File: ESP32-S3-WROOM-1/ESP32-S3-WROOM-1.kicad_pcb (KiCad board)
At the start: 2 copper layers, 25.4 x 57 mm, 23 parts, among them J1 ESP32-S3-DEVKITC-1-J1, J2 ESP32-S3-DEVKITC-1-J2, J3 UART, P1 USB2.0_C_12pin, SW1 BOOT, SW2 RESET, U1 ESP32-S3-WROOM-1, U2 AMS1117-3.3

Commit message: order
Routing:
- net GPIO8: track 18.3 -> 17.7 mm

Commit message: fix
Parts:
- removed P1: USB2.0_C_12pin, esp32-dev-boards:USB-C-12-Pin-MidMount
- added J4: USB2.0_C_v3, $74th:USB-C-12-Pin-MidMount-ali-v4, F.Cu at (77.5, 86.4)
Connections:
- D2 pad 2: GPIO20 -> GPIO19
- D3 pad 2: GPIO19 -> GPIO20
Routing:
- net GPIO19: track 66.4 -> 72.9 mm
- net GPIO20: track 68.1 -> 63.9 mm

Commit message: up
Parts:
- C1, C3, C4, C5, C6: footprint Capacitor_SMD:C_0805_2012Metric_Pad1.18x1.45mm_HandSolder -> esp32-dev-boards:Capacitor_0805_2012
- C2: value 100n -> 1u; footprint Capacitor_SMD:C_0805_2012Metric_Pad1.18x1.45mm_HandSolder -> esp32-dev-boards:Capacitor_0805_2012
- J3: value UART -> ESP-Prog-ProgramCOM-RECV; footprint esp32-dev-boards:UART -> $74th:BoxPinHeader_2x03_P1.27mm_Vertical
- R1, R2, R4: footprint Resistor_SMD:R_0805_2012Metric_Pad1.20x1.40mm_HandSolder -> esp32-dev-boards:Register_0805_2012
- R3: value 5.1k -> 1k; footprint Resistor_SMD:R_0805_2012Metric_Pad1.20x1.40mm_HandSolder -> esp32-dev-boards:Register_0805_2012
- moved J3 8.83 mm to (78.7, 79.2), turned to 90 degrees
- moved D1 5.56 mm to (85.0, 78.6), turned to 90 degrees
- moved D4 2.44 mm to (71.8, 80.5), turned to -90 degrees
- moved U2 0.23 mm to (74.5, 72.8)
- moved D3 0.12 mm to (83.7, 84.4)
- moved C2 0.06 mm to (82.1, 60.3)
- moved C4 0.06 mm to (68.9, 83.6)
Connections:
- J3 pad 1: U0TXD -> CHIP_PU
- J3 pad 2: U0RXD -> +5V
- J3 pad 3: +5V -> U0RXD
- J3 pad 5: CHIP_PU -> U0TXD
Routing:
- net Net-(D1-Pad2): track 12.8 -> 24.1 mm
- net U0TXD: track 55.6 -> 47.8 mm
- net GND: track 4.60 -> 11.2 mm, vias 14 -> 21
- net CHIP_PU: track 63.8 -> 69.0 mm
- net U0RXD: track 53.8 -> 49.2 mm
- net GPIO20: track 63.9 -> 61.5 mm
- net +5V: track 30.7 -> 29.1 mm
- net GPIO19: track 72.9 -> 71.9 mm
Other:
- board text added: "ESP32-S3-DevBoard v1.1.0"
- board text added: "JLCJLCJLCJLC"

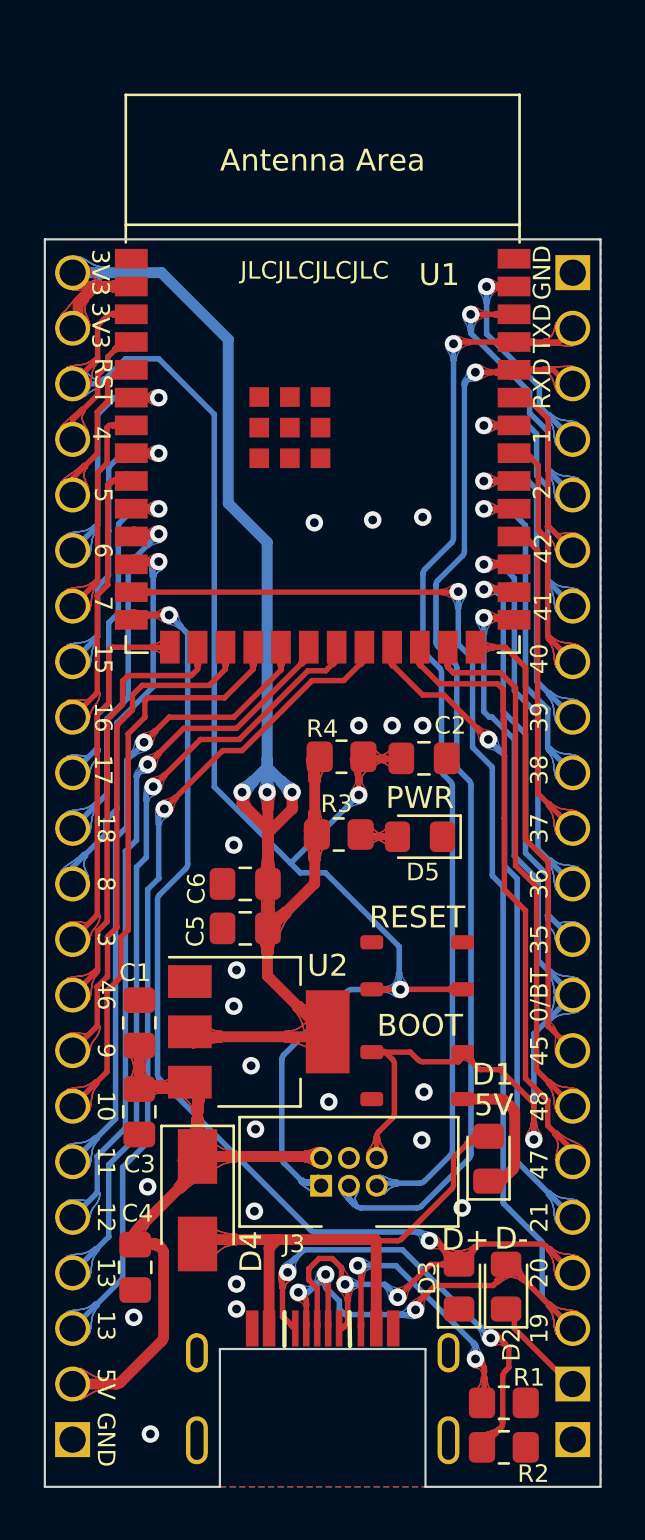
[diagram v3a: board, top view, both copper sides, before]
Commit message: ESP32-C3-WROOM-02
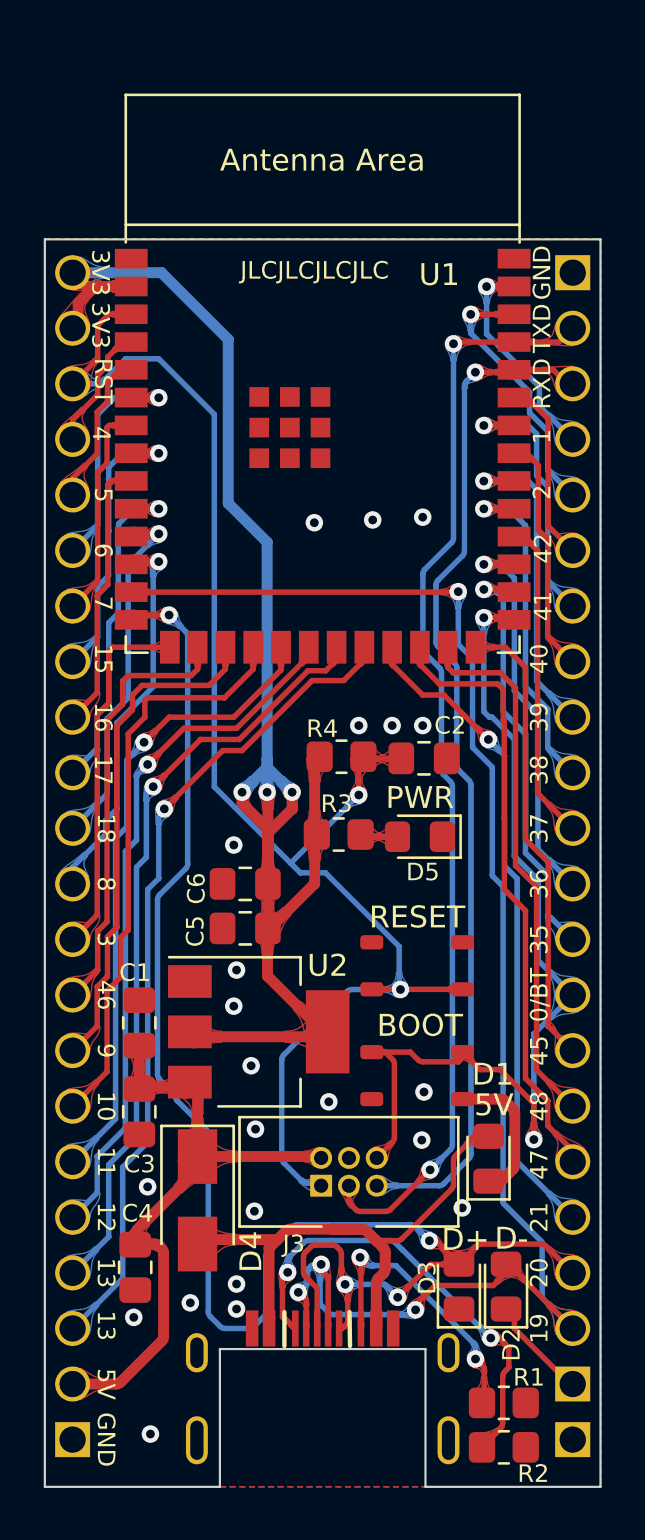
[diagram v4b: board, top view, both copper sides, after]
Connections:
- J3 pad 3: U0RXD -> U0TXD
- J3 pad 5: U0TXD -> U0RXD
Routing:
- net GPIO20: track 61.5 -> 73.6 mm
- net U0TXD: track 47.8 -> 50.4 mm, vias 1 -> 2
- net U0RXD: track 49.2 -> 46.7 mm
- net GPIO19: track 71.9 -> 73.7 mm
- net Net-(D1-Pad2): track 24.1 -> 25.9 mm
- net Net-(J4-Pad5): track 20.4 -> 20.9 mm
- net GND: vias 21 -> 22
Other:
- board text added: "ESP32-S3-DevBoard v1.1.1"
- board text removed: "ESP32-S3-DevBoard v1.1.0"

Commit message: fix D1, IO14
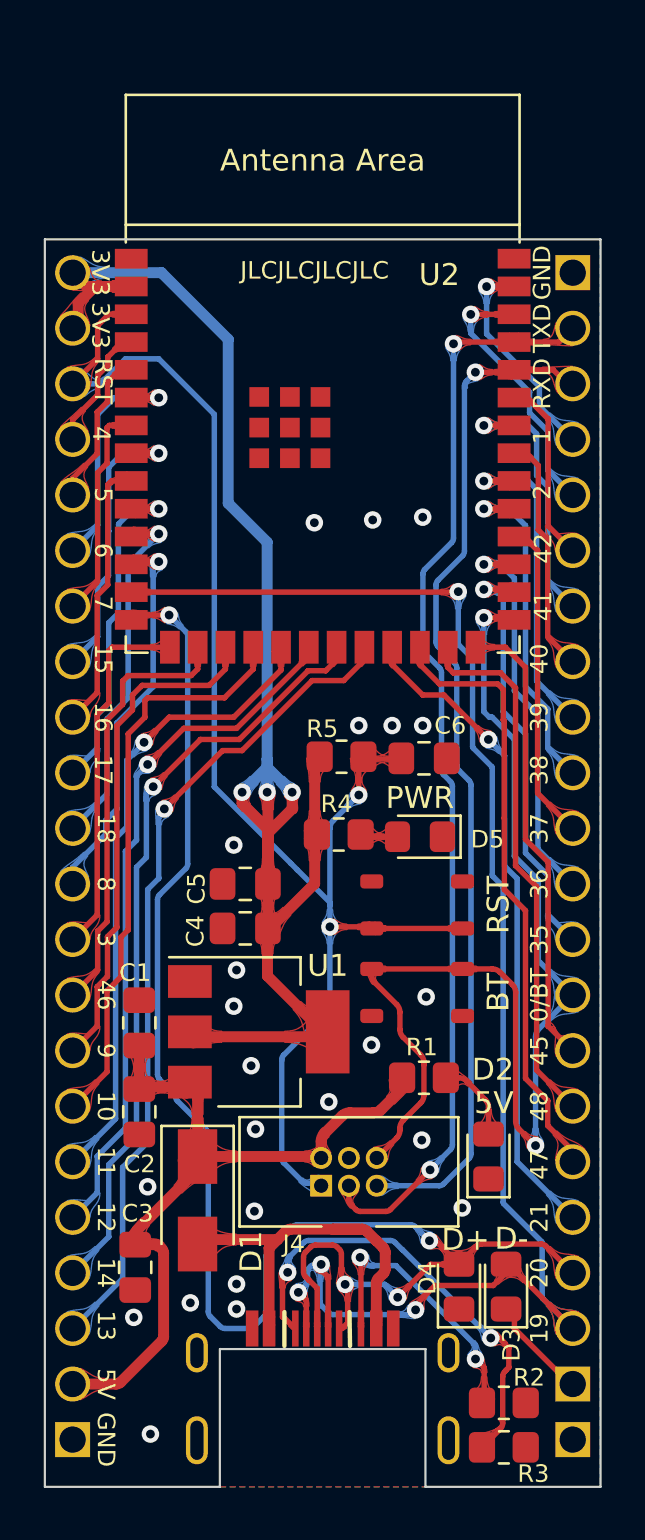
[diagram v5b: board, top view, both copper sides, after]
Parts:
- added R1: 1k, esp32-dev-boards:Register_0805_2012, F.Cu at (82.0, 75.0)
- SW1: value BOOT -> BT
- SW2: value RESET -> RST
- moved SW1 3.80 mm to (81.8, 71.0)
- moved SW2 2.78 mm to (81.8, 67.0)
- moved D2 0.10 mm to (85.0, 78.5)
- renumbered C3 to C2, C4 to C3, C5 to C4, C6 to C5, C2 to C6, D4 to D1, D1 to D2, D2 to D3, D3 to D4, J4 to J3, J3 to J4, R1 to R2, R2 to R3, R3 to R4, R4 to R5, U2 to U1, U1 to U2
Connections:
- D2 pad 2: Net-(D1-Pad2) -> Net-(D2-Pad2)
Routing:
- net GPIO0: track 43.5 -> 52.8 mm
- net Net-(D1-Pad2): track 25.9 -> 18.0 mm
- net GND: track 11.2 -> 4.60 mm, vias 22 -> 23
- net +5V: track 29.1 -> 35.1 mm
- net Net-(D2-Pad2): track 0.00 -> 3.80 mm
- net CHIP_PU: track 69.0 -> 67.4 mm
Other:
- board text added: "14"
- board text added: "ESP32-S3-DevBoard v1.1.2"
- board text removed: "ESP32-S3-DevBoard v1.1.1"

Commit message: new ver
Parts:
- removed the C1 at (69.1, 72.4)
- removed the D2 at (85.0, 78.5)
- removed D3: D-, LED_SMD:LED_0805_2012Metric_Pad1.15x1.40mm_HandSolder
- removed D4: D+, LED_SMD:LED_0805_2012Metric_Pad1.15x1.40mm_HandSolder
- removed the J3 at (77.5, 86.4)
- removed the R1 at (82.0, 75.0)
- added G***: LOGO, $74th:74th-7.5mm, B.Cu at (81.3, 66.8)
- added J4: USB2.0_C_v3, $74th:USB-C-12-Pin-SMD, F.Cu at (77.3, 89.0)
- added REF**: twitter, $74th:twitter, B.Cu at (81.3, 59.7)
- C1: renamed from C6; moved to B.Cu
- C2: renamed from C5; moved to B.Cu
- C3: renamed from C4; moved to B.Cu
- C5: renamed from C2; moved to B.Cu
- C6: renamed from C3; moved to B.Cu
- J1: footprint esp32-dev-boards:ESP32-S3-DEVKITC-J1 -> esp32-dev-boards:ESP32-S3-DEVKITC-J1-mini
- J2: footprint esp32-dev-boards:ESP32-S3-DEVKITC-J2 -> esp32-dev-boards:ESP32-S3-DEVKITC-J2-mini
- R1: renamed from R5; moved to B.Cu
- R2: renamed from R4; moved to B.Cu
- R3: renamed from R2; moved to B.Cu
- R4: renamed from R3; moved to B.Cu
- SW1: renamed from SW2; value RST -> RS
- moved C3 27.8 mm to (73.3, 40.3), turned to 0 degrees
- moved C2 23.6 mm to (73.3, 42.4), turned to 0 degrees
- moved C1 16.1 mm to (74.7, 46.0)
- moved R1 12.7 mm to (74.8, 48.1), turned to 0 degrees
- moved R3 10.5 mm to (75.4, 88.4), turned to -90 degrees
- moved C6 7.77 mm to (75.2, 79.0)
- moved R4 7.61 mm to (79.0, 88.4), turned to -90 degrees
- moved C5 4.58 mm to (72.9, 79.0)
- moved SW1 3.43 mm to (82.0, 70.4)
- moved SW2 3.43 mm to (82.0, 74.4)
- moved U1 2.42 mm to (77.5, 48.1)
- moved D2 1.42 mm to (70.4, 80.8)
- renumbered D5 to D1, D1 to D2, J4 to J3, SW1 to SW2, U2 to U1, U1 to U2
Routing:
- net GPIO19: track 73.7 -> 0.00 mm, vias 4 -> 0
- net GPIO20: track 73.6 -> 0.00 mm, vias 4 -> 0
- net CHIP_PU: track 67.4 -> 0.00 mm, vias 2 -> 0
- net GPIO0: track 52.8 -> 0.00 mm, vias 2 -> 0
- net U0TXD: track 50.4 -> 0.00 mm, vias 2 -> 0
- net U0RXD: track 46.7 -> 0.00 mm, vias 1 -> 0
- net GPIO14: track 38.0 -> 0.00 mm, vias 1 -> 0
- net GPIO13: track 35.1 -> 0.00 mm, vias 1 -> 0
- net GPIO12: track 31.9 -> 0.00 mm, vias 1 -> 0
- net GPIO21: track 30.0 -> 0.00 mm, vias 1 -> 0
- net GPIO11: track 29.2 -> 0.00 mm, vias 1 -> 0
- net GPIO47: track 28.0 -> 0.00 mm
- net GPIO10: track 26.4 -> 0.00 mm
- net +3V3: track 76.1 -> 50.0 mm, vias 3 -> 2
- net GPIO48: track 24.6 -> 0.00 mm
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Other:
- board size 25.4 x 57 mm -> 25.4 x 53.2 mm
- board text added: "0"
- board text added: "3V"
- board text added: "DevBoard"
- board text added: "ESP32-S3"
- board text added: "G"
- board text added: "RS"
- board text added: "RX"
- board text added: "TX"
- board text added: "v1.2.0"
- board text removed: "0/BT"
- board text removed: "3V3"
- board text removed: "ESP32-S3-DevBoard v1.1.2"
- board text removed: "GND"
- board text removed: "RST"
- board text removed: "RXD"
- board text removed: "TXD"

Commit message: new ver
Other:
- board size 25.4 x 53.2 mm -> 25.4 x 51.3 mm
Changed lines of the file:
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@@
   (gr_line (start 88.9 90.424) (end 66.04 90.424)
     (stroke (width 0.1) (type solid)) (layer "Edge.Cuts"))
-  (gr_line (start 64.77 89.154) (end 64.77 37.211)
+  (gr_line (start 64.77 89.154) (end 64.77 40.386)
     (stroke (width 0.1) (type solid)) (layer "Edge.Cuts"))
   (gr_arc (start 90.17 89.154) (mid 89.798026 90.052026) (end 88.9 90.424)
     (stroke (width 0.1) (type default)) (layer "Edge.Cuts"))
-  (gr_line (start 90.17 40.132) (end 90.17 89.154)
+  (gr_line (start 90.17 40.386) (end 90.17 89.154)
     (stroke (width 0.1) (type solid)) (layer "Edge.Cuts"))
   (gr_line (start 66.04 39.116) (end 88.9 39.116)

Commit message: v1.2.0
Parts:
- moved G*** 1.77 mm to (82.9, 67.4)
- renumbered C3 to C1, C1 to C3, C6 to C4, R4 to R3, R3 to R4
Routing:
- net GPIO20: track 0.00 -> 67.9 mm, vias 0 -> 2
- net GPIO19: track 0.00 -> 61.7 mm, vias 0 -> 2
- net CHIP_PU: track 0.00 -> 60.7 mm, vias 0 -> 3
- net GPIO0: track 0.00 -> 59.3 mm, vias 0 -> 1
- net U0TXD: track 0.00 -> 52.7 mm
- net U0RXD: track 0.00 -> 49.2 mm, vias 0 -> 1
- net GPIO14: track 0.00 -> 35.7 mm
- net GPIO13: track 0.00 -> 31.0 mm, vias 0 -> 1
- net GPIO21: track 0.00 -> 30.9 mm
- net GPIO12: track 0.00 -> 28.0 mm, vias 0 -> 1
- net GND: track 0.00 -> 26.3 mm, vias 2 -> 29
- net GPIO11: track 0.00 -> 25.0 mm, vias 0 -> 1
- net GPIO47: track 0.00 -> 23.9 mm, vias 0 -> 1
- net GPIO10: track 0.00 -> 21.9 mm, vias 0 -> 1
- net GPIO48: track 0.00 -> 20.9 mm
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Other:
- board text added: "T"
- board text added: "V"
- board text removed: "3V"
- board text removed: "TX"
